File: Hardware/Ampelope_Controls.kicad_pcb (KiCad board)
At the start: 2 copper layers, 60.5 x 110 mm, 36 parts, among them J1 Conn_01x12_Male, J10 Audio2_In, J11 Audio3_In, J12 Audio4_In, J13 Audio1_Out, J14 Audio2_Out, J15 Audio3_Out, J16 Audio4_Out, J17 Clock_In, J18 Env1_Out, J19 Env3_Out, J2 Conn_01x12_Male, J3 Conn_01x12_Male, J4 Conn_01x12_Male, J5 Gate1_In, J6 Gate2_In, J7 Gate3_In, J8 Gate4_In, J9 Audio1_In

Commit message: Various schematic and PCB tidying
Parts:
- moved J2 0.50 mm to (158.5, 101.1)
- renumbered E1A_POT1 to EnvA_A_POT1, E1D_POT1 to EnvA_D_POT1, E1R_POT1 to EnvA_R_POT1, E1S_POT1 to EnvA_S_POT1, E2A_POT1 to EnvB_A_POT1, E2D_POT1 to EnvB_D_POT1, E2R_POT1 to EnvB_R_POT1, E2S_POT1 to EnvB_S_POT1
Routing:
- net /Audio3_Out: track 82.6 -> 81.8 mm
- net /Env4_LFO: track 55.2 -> 54.5 mm
- net /EnvB_Sustain: track 70.2 -> 69.6 mm
- net /Led3_Out: track 47.1 -> 46.5 mm
- net /Gate4_In: track 57.3 -> 56.8 mm
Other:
- board text added: "Ampelope Controls v1.0 Mountjoy Modular 2021"

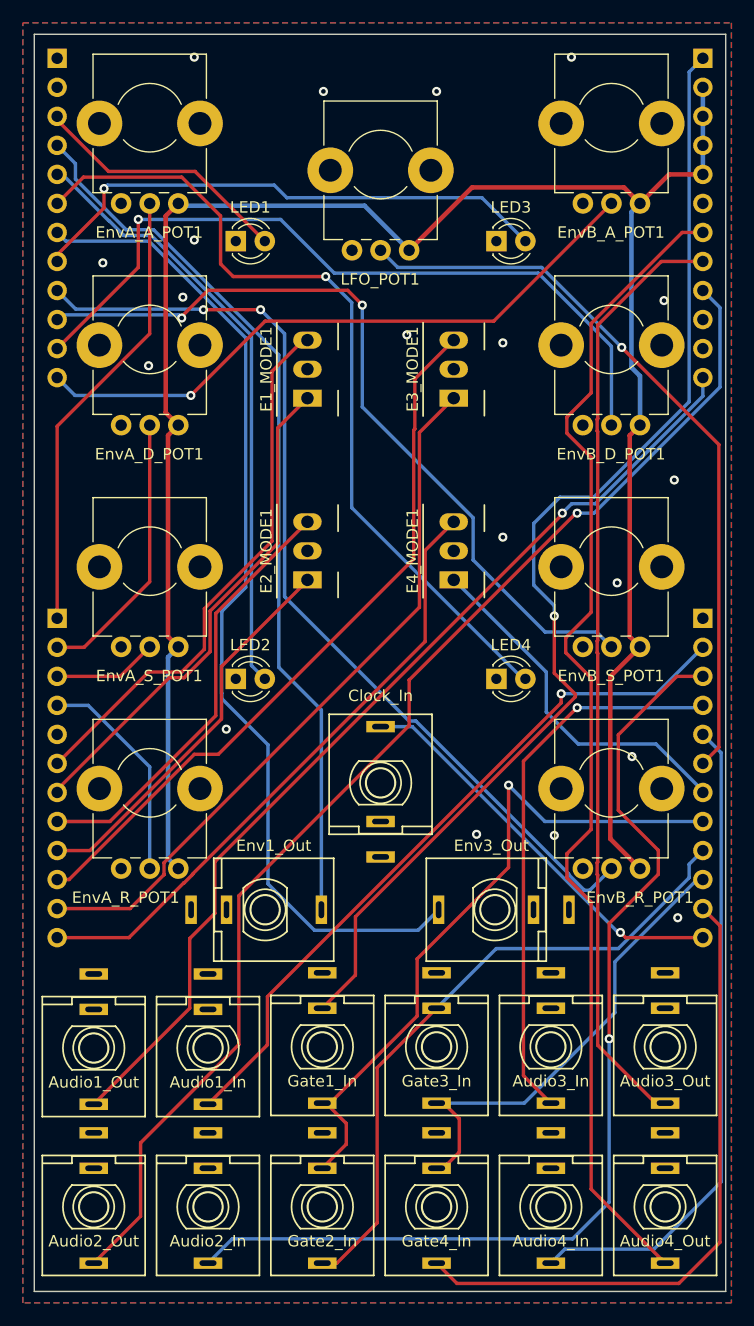
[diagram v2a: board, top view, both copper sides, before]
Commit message: Changed input protection diodes back to 3904s; prepared gerbers
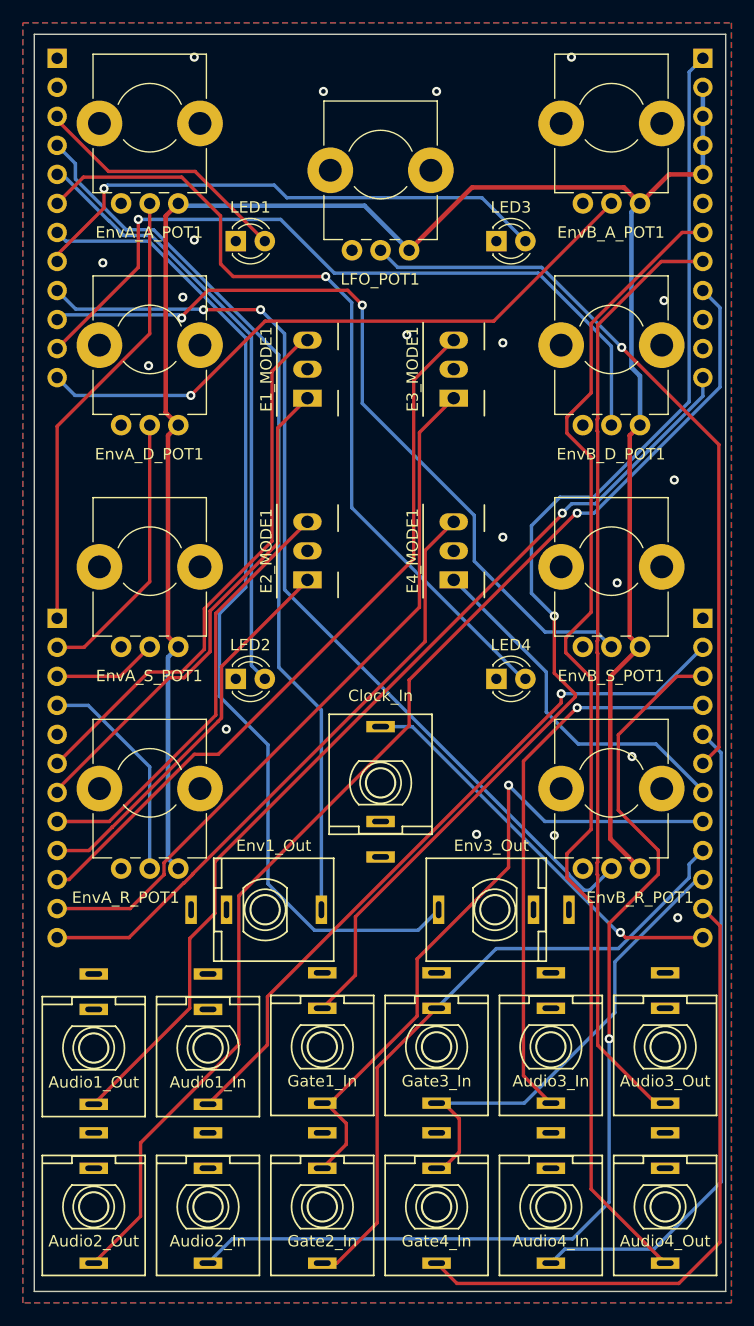
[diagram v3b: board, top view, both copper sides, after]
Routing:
- net /Gate3_In: track 40.9 -> 40.4 mm
